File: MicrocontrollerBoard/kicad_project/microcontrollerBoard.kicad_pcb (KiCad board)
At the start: 2 copper layers, 78.7 x 63.5 mm, 55 parts, among them J1 PROG_CONN, J10 PC_5V, J13 PA_GND, J14 PB_GND, J15 PC_GND, J18 COM, J19 COM_5V, J2 5V_CONN, J20 COM_GND, J21 POWER_CONN, J22 MOTOR2, J23 MOTOR1, J3 PA, J4 PB, J5 PC, J6 3V_CONN_1, J7 3V_CONN_2, J8 PA_5V, J9 PB_5V, U1 ATmega1284P-PU, U2 TC4422, U3 TC4422, U4 TC4422, U5 TC4422, U6 AMS1117-3.3, Y1 16MHz

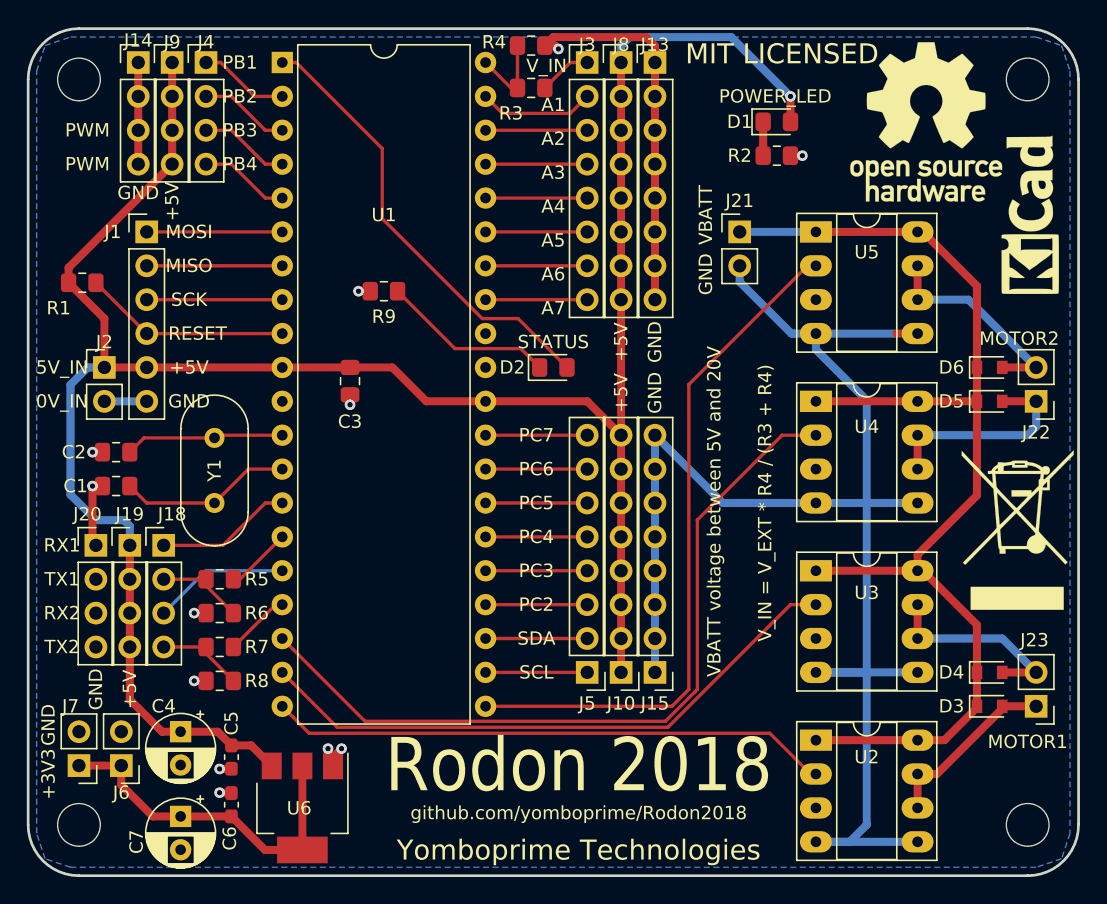
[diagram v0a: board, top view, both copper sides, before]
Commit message: uC board: Added resistors to MISO, brought out a RESET pin, minor fixes.
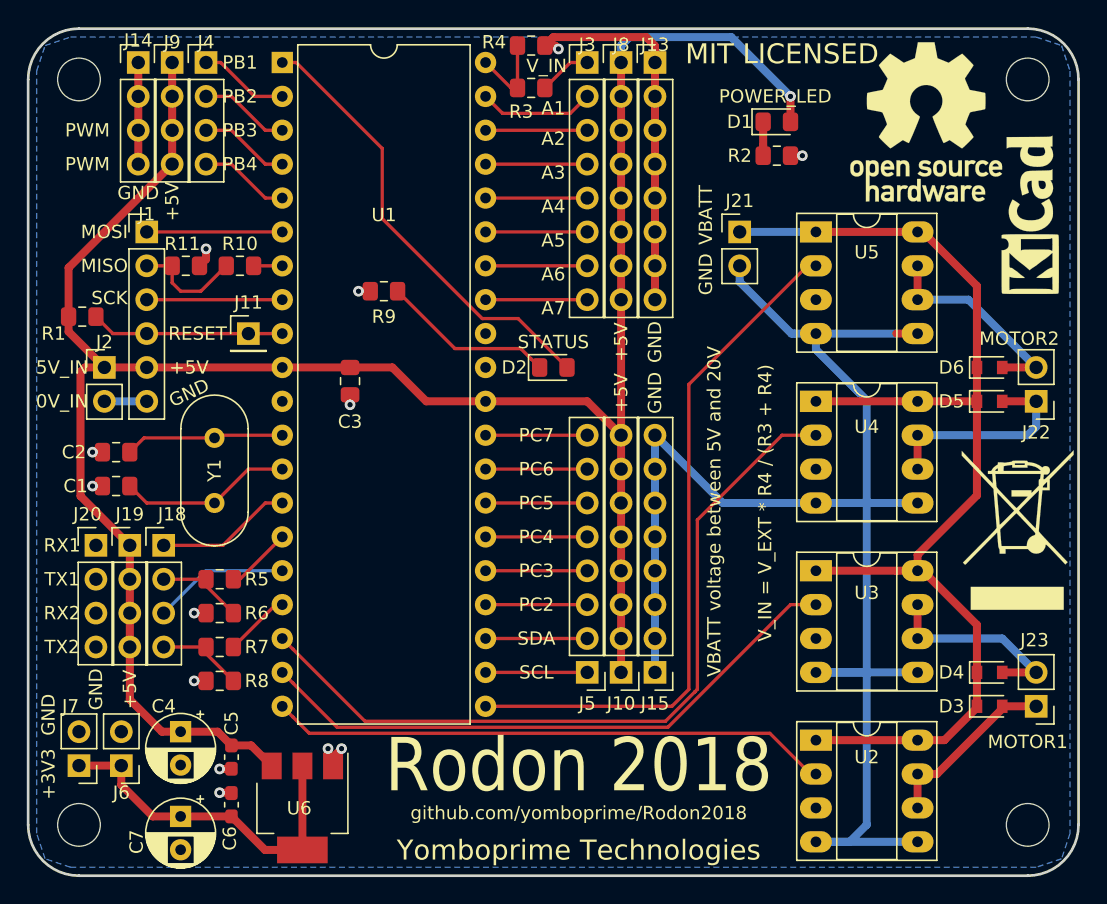
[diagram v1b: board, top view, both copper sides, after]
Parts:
- added J11: CONN_RESET, Connector_PinHeader_2.54mm:PinHeader_1x01_P2.54mm_Vertical, F.Cu at (91.4, 73.7)
- added R10: R, Resistor_SMD:R_0805_2012Metric_Pad1.15x1.40mm_HandSolder, F.Cu at (90.8, 68.6)
- added R11: R, Resistor_SMD:R_0805_2012Metric_Pad1.15x1.40mm_HandSolder, F.Cu at (86.8, 68.6)
- moved R1 2.54 mm to (79.0, 72.4)
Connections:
- J1 pad 2: MISO -> Net-(J1-Pad2)
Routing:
- net Net-(J1-Pad2): track 0.00 -> 8.28 mm
- net MISO: track 10.2 -> 2.15 mm
- net GND: track 176.4 -> 173.7 mm, vias 12 -> 13
- net +5V: track 174.2 -> 172.4 mm
- net RESET: track 15.5 -> 14.5 mm

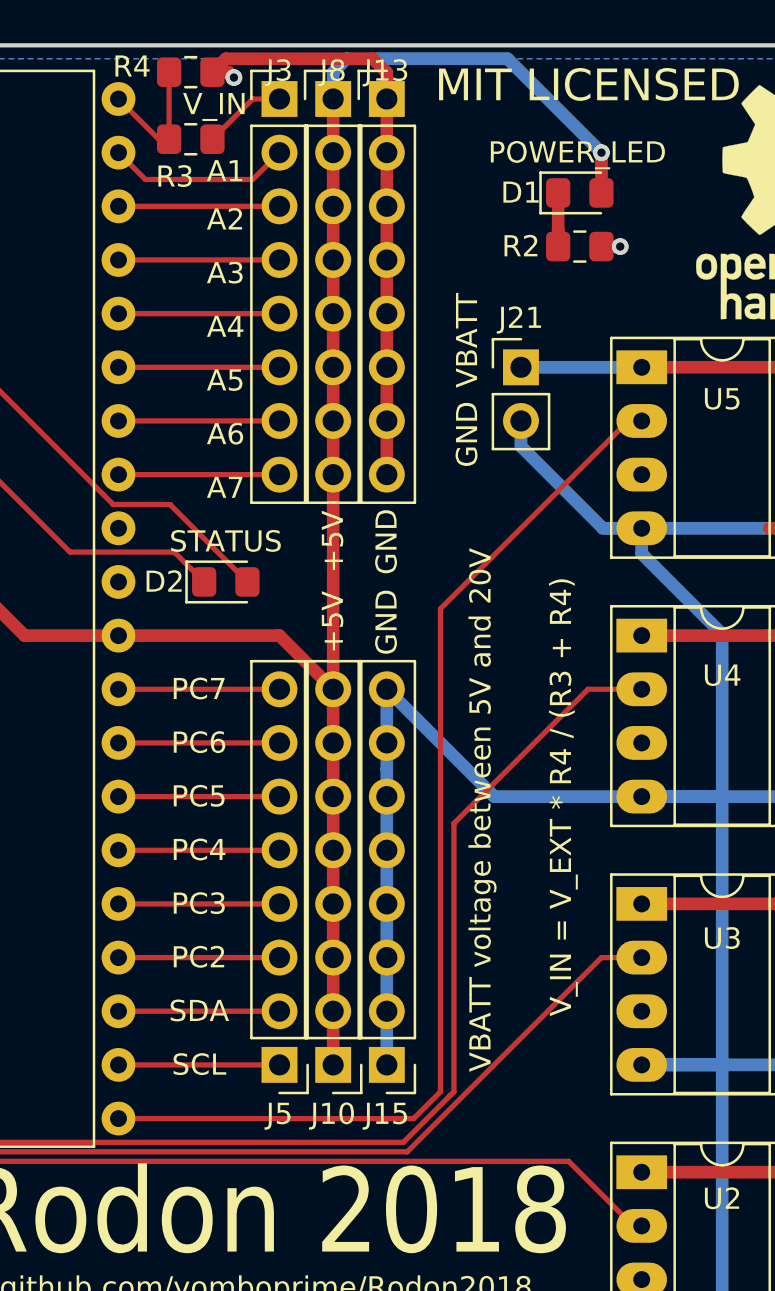
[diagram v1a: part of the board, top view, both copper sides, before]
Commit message: uC board: V_IN is no longer exposed. Better power routing.
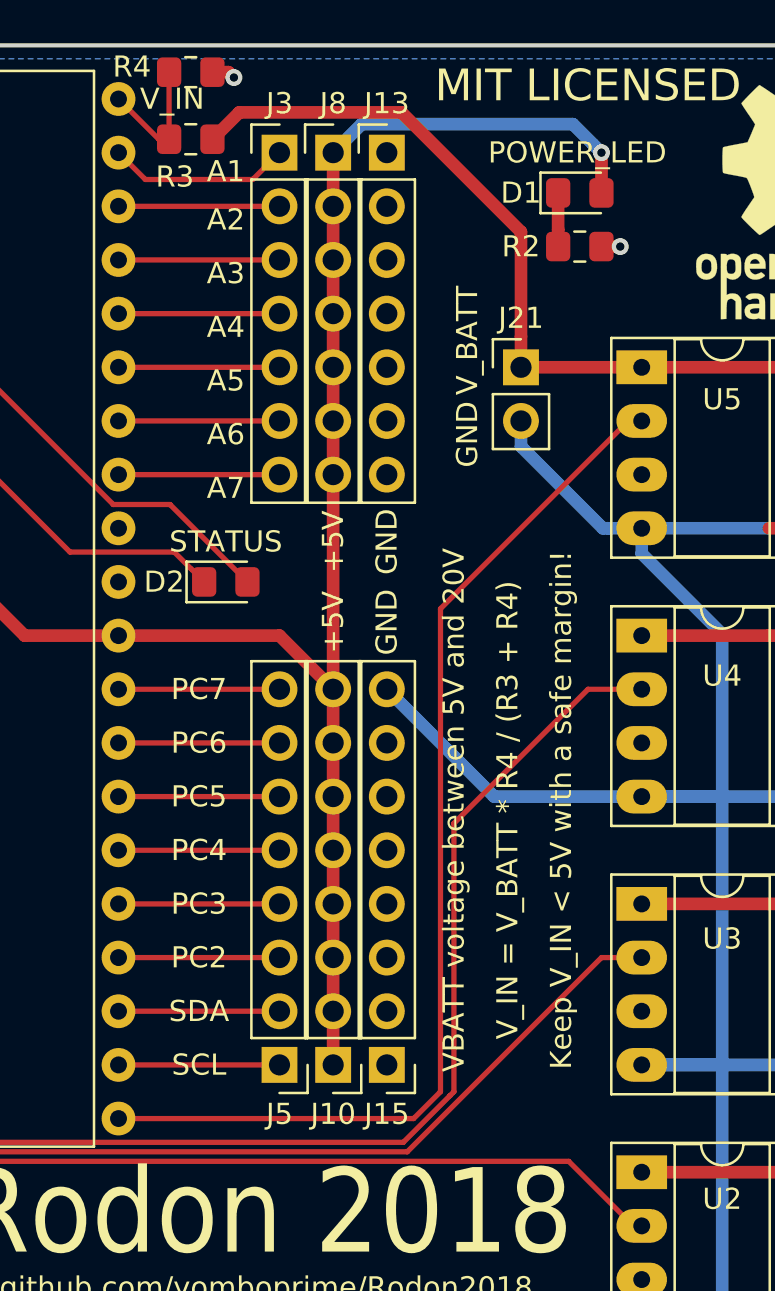
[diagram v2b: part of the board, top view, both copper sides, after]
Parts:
- J13, J3, J8: footprint Connector_PinHeader_2.54mm:PinHeader_1x08_P2.54mm_Vertical -> Connector_PinHeader_2.54mm:PinHeader_1x07_P2.54mm_Vertical
- R10: value R -> 1K
- R11: value R -> 2K
- moved J13 2.54 mm to (121.9, 55.9)
- moved J3 2.54 mm to (116.8, 55.9)
- moved J8 2.54 mm to (119.4, 55.9)
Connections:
- J3 pad 1: V_EXT -> Net-(J3-Pad1)
- R3 pad 1: V_EXT -> +BATT
- U1 pad 33: Net-(J3-Pad8) -> Net-(J3-Pad7)
- U1 pad 34: Net-(J3-Pad7) -> Net-(J3-Pad6)
- U1 pad 35: Net-(J3-Pad6) -> Net-(J3-Pad5)
- U1 pad 36: Net-(J3-Pad5) -> Net-(J3-Pad4)
- U1 pad 37: Net-(J3-Pad4) -> Net-(J3-Pad3)
- U1 pad 38: Net-(J3-Pad3) -> Net-(J3-Pad2)
- U1 pad 39: Net-(J3-Pad2) -> Net-(J3-Pad1)
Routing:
- net GND: track 173.7 -> 128.1 mm
- net +BATT: track 87.8 -> 111.6 mm
- net Net-(J3-Pad1): track 0.00 -> 8.67 mm
- net Net-(J3-Pad8): track 7.62 -> 0.00 mm
- net +5V: track 172.4 -> 167.6 mm
- net V_EXT: track 3.96 -> 0.00 mm
- net Net-(J3-Pad2): track 8.67 -> 7.62 mm
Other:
- board text added: "Keep V_IN < 5V with a safe margin!"
- board text added: "V_BATT"
- board text added: "V_IN = V_BATT * R4 / (R3 + R4)"
- board text removed: "VBATT"
- board text removed: "V_IN = V_EXT * R4 / (R3 + R4)"

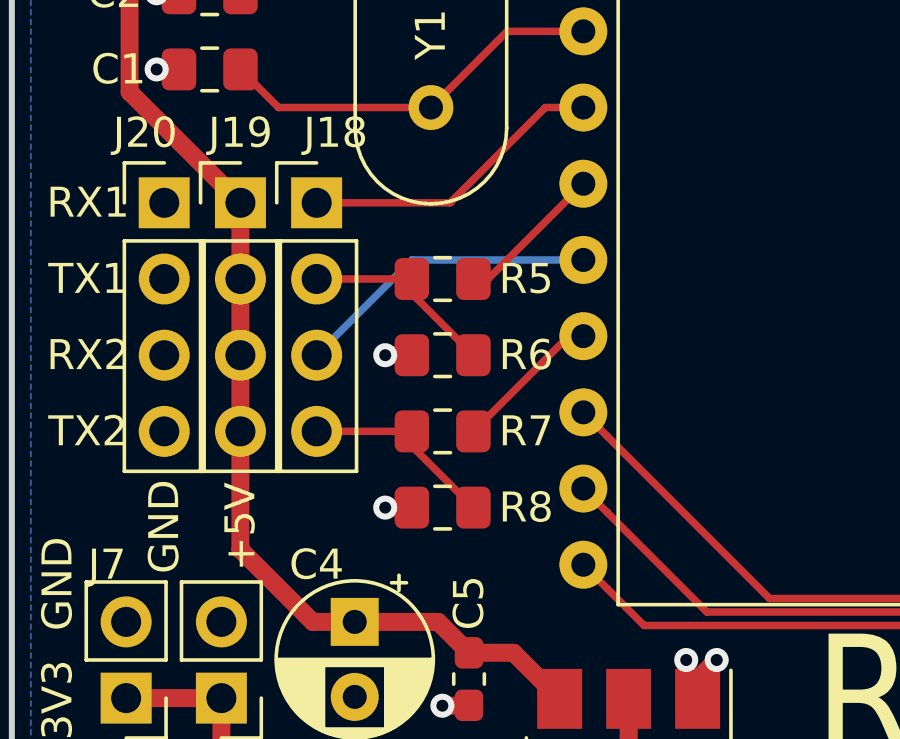
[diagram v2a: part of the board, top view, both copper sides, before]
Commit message: uC board: better ground plane connection.
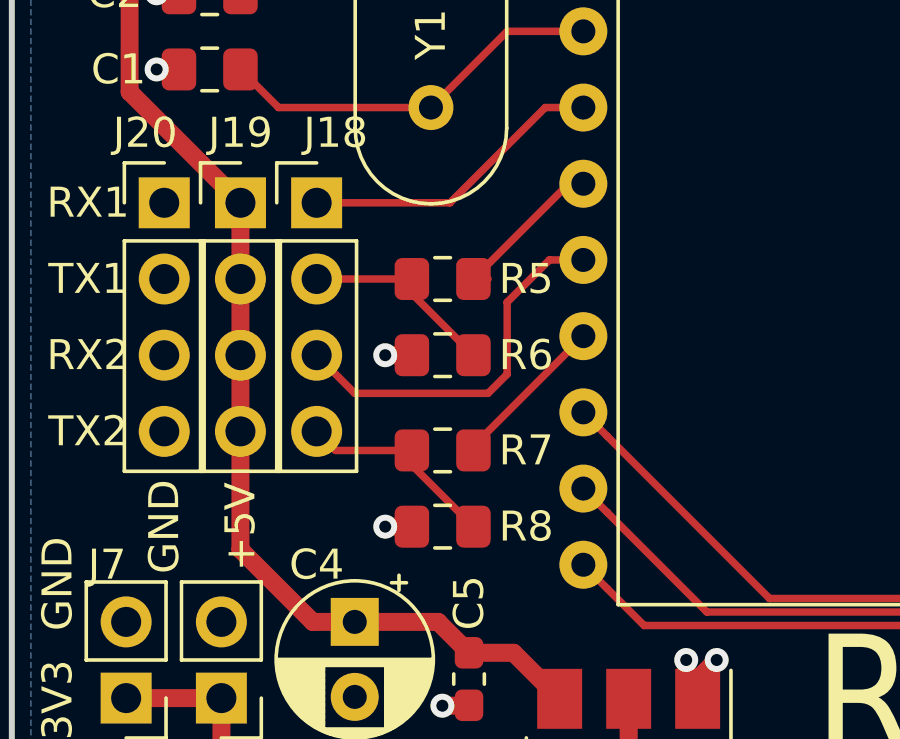
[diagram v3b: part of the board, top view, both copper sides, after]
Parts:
- moved R7 0.64 mm to (89.3, 97.8)
- moved R8 0.64 mm to (89.3, 100.3)
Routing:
- net RX2: track 10.2 -> 12.7 mm
- net TX2_INT: track 4.98 -> 5.82 mm
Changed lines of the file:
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@@
     (thickness 1.6)
     (drawings 65)
-    (tracks 265)
+    (tracks 272)
     (zones 0)
     (modules 58)
@@
   )
   (module Resistor_SMD:R_0805_2012Metric_Pad1.15x1.40mm_HandSolder (layer F.Cu)
-    (at 89.29 97.155 180)
+    (at 89.29 97.79 180)
     (descr "Resistor SMD 0805 (2012 Metric), square (rectangular) end terminal, IPC_7351 nominal with elongated pad for handsoldering. (Body size source: https://docs.google.com/spreadsheets/d/1BsfQQcO9C6DZCsRaXUlFlo91Tg2WpOkGARC1WS5S8t0/edit?usp=sharing), generated with kicad-footprint-generator")
     (tags "resistor handsolder")
@@
   )
   (module Resistor_SMD:R_0805_2012Metric_Pad1.15x1.40mm_HandSolder (layer F.Cu)
-    (at 89.29 99.695 180)
+    (at 89.29 100.33 180)
     (descr "Resistor SMD 0805 (2012 Metric), square (rectangular) end terminal, IPC_7351 nominal with elongated pad for handsoldering. (Body size source: https://docs.google.com/spreadsheets/d/1BsfQQcO9C6DZCsRaXUlFlo91Tg2WpOkGARC1WS5S8t0/edit?usp=sharing), generated with kicad-footprint-generator")
     (tags "resistor handsolder")
@@
   (segment (start 80.645 82.405) (end 80.5 82.55) (width 0.6) (layer F.Cu) (net 1))
   (via (at 87.376 94.615) (size 0.8) (drill 0.4) (layers F.Cu B.Cu) (net 1))
-  (via (at 87.376 99.695) (size 0.8) (drill 0.4) (layers F.Cu B.Cu) (net 1))
+  (via (at 87.376 100.33) (size 0.8) (drill 0.4) (layers F.Cu B.Cu) (net 1))
   (segment (start 141.605 111.76) (end 133.985 111.76) (width 0.6) (layer B.Cu) (net 1))
   (segment (start 141.605 99.06) (end 133.985 99.06) (width 0.6) (layer B.Cu) (net 1))
@@
   (segment (start 128.27 69.782081) (end 132.147919 73.66) (width 0.6) (layer B.Cu) (net 1))
   (segment (start 128.27 68.58) (end 128.27 69.782081) (width 0.6) (layer B.Cu) (net 1))
-  (segment (start 87.376 99.695) (end 88.265 99.695) (width 0.6) (layer F.Cu) (net 1))
   (segment (start 87.376 94.615) (end 88.265 94.615) (width 0.6) (layer F.Cu) (net 1))
   (segment (start 99.06 78.994) (end 99.06 78.25) (width 0.6) (layer F.Cu) (net 1))
@@
   (segment (start 88.265 68.09) (end 87.775 68.58) (width 0.6) (layer F.Cu) (net 1))
   (segment (start 88.265 67.31) (end 88.265 68.09) (width 0.6) (layer F.Cu) (net 1))
+  (segment (start 87.376 100.33) (end 88.265 100.33) (width 0.6) (layer F.Cu) (net 1))
   (segment (start 91.44 83.82) (end 88.9 86.36) (width 0.25) (layer F.Cu) (net 2))
   (segment (start 93.98 83.82) (end 91.44 83.82) (width 0.25) (layer F.Cu) (net 2))
@@
   (segment (start 109.22 99.06) (end 116.84 99.06) (width 0.25) (layer F.Cu) (net 27))
   (segment (start 109.22 96.52) (end 116.84 96.52) (width 0.25) (layer F.Cu) (net 28))
-  (segment (start 88.265 97.645) (end 88.265 97.155) (width 0.25) (layer F.Cu) (net 29))
-  (segment (start 90.315 99.695) (end 88.265 97.645) (width 0.25) (layer F.Cu) (net 29))
-  (segment (start 88.265 97.155) (end 85.09 97.155) (width 0.25) (layer F.Cu) (net 29))
-  (segment (start 88.265 91.44) (end 93.98 91.44) (width 0.25) (layer B.Cu) (net 30))
-  (segment (start 85.09 94.615) (end 88.265 91.44) (width 0.25) (layer B.Cu) (net 30))
+  (segment (start 85.725 97.79) (end 85.09 97.155) (width 0.25) (layer F.Cu) (net 29))
+  (segment (start 88.265 97.79) (end 85.725 97.79) (width 0.25) (layer F.Cu) (net 29))
+  (segment (start 88.265 98.28) (end 88.265 97.79) (width 0.25) (layer F.Cu) (net 29))
+  (segment (start 90.315 100.33) (end 88.265 98.28) (width 0.25) (layer F.Cu) (net 29))
+  (segment (start 91.44 95.25) (end 90.805 95.885) (width 0.25) (layer F.Cu) (net 30))
+  (segment (start 91.44 92.84863) (end 91.44 95.25) (width 0.25) (layer F.Cu) (net 30))
+  (segment (start 93.98 91.44) (end 92.84863 91.44) (width 0.25) (layer F.Cu) (net 30))
+  (segment (start 86.36 95.885) (end 85.09 94.615) (width 0.25) (layer F.Cu) (net 30))
+  (segment (start 90.805 95.885) (end 86.36 95.885) (width 0.25) (layer F.Cu) (net 30))
+  (segment (start 92.84863 91.44) (end 91.44 92.84863) (width 0.25) (layer F.Cu) (net 30))
   (segment (start 88.265 92.565) (end 88.265 92.075) (width 0.25) (layer F.Cu) (net 31))
   (segment (start 90.315 94.615) (end 88.265 92.565) (width 0.25) (layer F.Cu) (net 31))
@@
   (segment (start 111.615 55.245) (end 111.615 52.07) (width 0.25) (layer F.Cu) (net 33))
   (segment (start 90.805 92.075) (end 90.315 92.075) (width 0.25) (layer F.Cu) (net 34))
-  (segment (start 93.98 88.9) (end 90.805 92.075) (width 0.25) (layer F.Cu) (net 34))
+  (segment (start 93.49 88.9) (end 93.98 88.9) (width 0.25) (layer F.Cu) (net 34))
+  (segment (start 90.315 92.075) (end 93.49 88.9) (width 0.25) (layer F.Cu) (net 34))
   (segment (start 93.49 93.98) (end 93.98 93.98) (width 0.25) (layer F.Cu) (net 35))
-  (segment (start 90.315 97.155) (end 93.49 93.98) (width 0.25) (layer F.Cu) (net 35))
+  (segment (start 90.315 97.645) (end 90.315 97.79) (width 0.25) (layer F.Cu) (net 35))
+  (segment (start 93.98 93.98) (end 90.315 97.645) (width 0.25) (layer F.Cu) (net 35))
   (segment (start 130.530021 103.625021) (end 96.005021 103.625021) (width 0.25) (layer F.Cu) (net 36))
   (segment (start 94.779999 102.399999) (end 93.98 101.6) (width 0.25) (layer F.Cu) (net 36))
